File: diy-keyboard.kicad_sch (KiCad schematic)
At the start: 21 parts, among them J1 AVR-ISP-6, SW69 SW_SKQG, U1 PRTR5V0U2X, U2 ATmega32U4-A, Y1 16MHz

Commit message: Re-assign symbol and footprint to match local library
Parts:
- J1: footprint Local_lib_ISP-header:Reset_Pretty-Mask -> Local_Lib:Reset_Pretty-Mask
- USB1: footprint Local_lib_Type-C:HRO-TYPE-C-31-M-12-HandSoldering -> Local_Lib:HRO-TYPE-C-31-M-12-HandSoldering

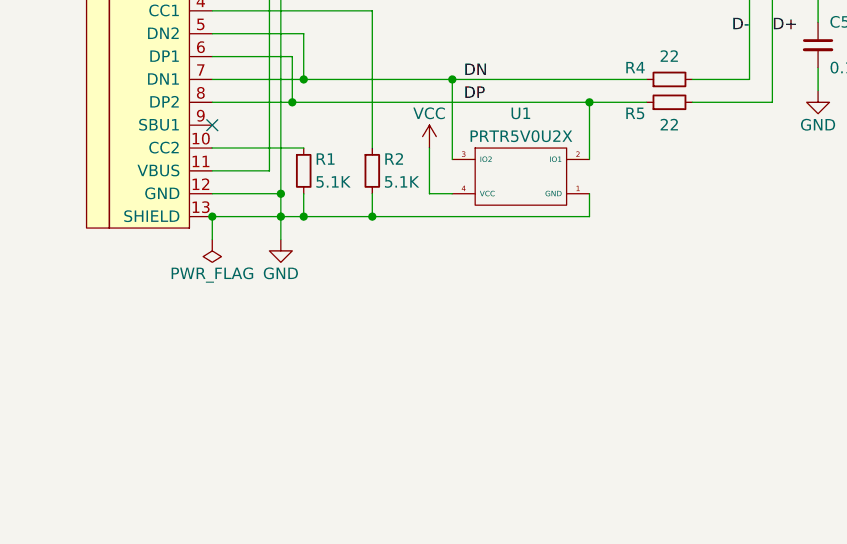
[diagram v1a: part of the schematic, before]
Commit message: Adding ferrite bead to usb sield
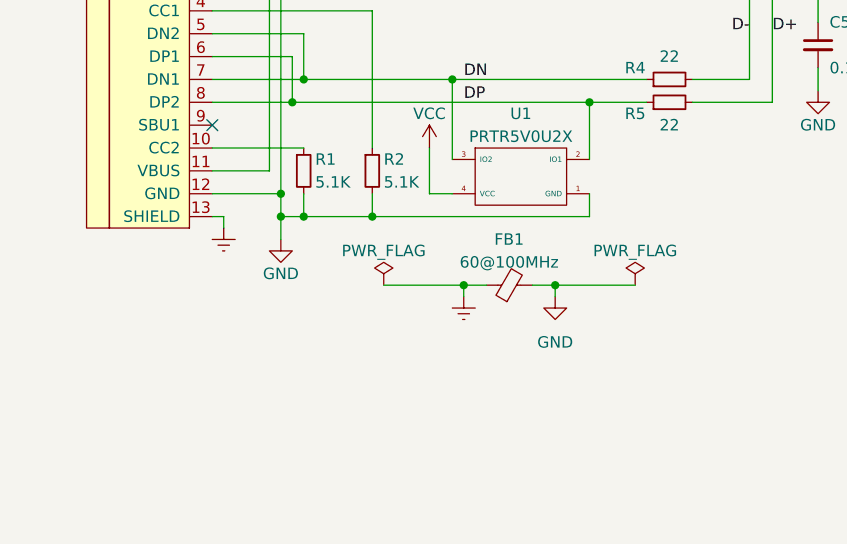
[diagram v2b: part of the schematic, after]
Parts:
- added FB1: 60@100MHz, Inductor_SMD:L_0805_2012Metric_Pad1.15x1.40mm_HandSolder, symbol Device:FerriteBead_Small
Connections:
- net GND: now also FB1.2; no longer USB1.13 (SHIELD)
- new net Earth: FB1.1, USB1.13 (SHIELD)
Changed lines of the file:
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@@
   (junction (at 67.31 120.65) (diameter 0) (color 0 0 0 0)
   )
+  (junction (at 87.63 128.27) (diameter 0) (color 0 0 0 0)
+  )
   (junction (at 104.14 80.01) (diameter 0) (color 0 0 0 0)
   )
@@
   (junction (at 104.14 77.47) (diameter 0) (color 0 0 0 0)
   )
+  (junction (at 97.79 128.27) (diameter 0) (color 0 0 0 0)
+  )
   (junction (at 86.36 92.71) (diameter 0) (color 0 0 0 0)
   )
@@
   )
   (junction (at 67.31 118.11) (diameter 0) (color 0 0 0 0)
-  )
-  (junction (at 59.69 120.65) (diameter 0) (color 0 0 0 0)
   )
   (junction (at 147.32 147.32) (diameter 0) (color 0 0 0 0)
@@
     (stroke (width 0) (type default))
   )
+  (wire (pts (xy 87.63 128.27) (xy 87.63 129.54))
+    (stroke (width 0) (type default))
+  )
   (wire (pts (xy 86.36 90.17) (xy 86.36 92.71))
     (stroke (width 0) (type default))
@@
     (stroke (width 0) (type default))
   )
-  (wire (pts (xy 67.31 120.65) (xy 59.69 120.65))
-    (stroke (width 0) (type default))
-  )
   (wire (pts (xy 163.83 116.84) (xy 173.99 116.84))
     (stroke (width 0) (type default))
@@
     (stroke (width 0) (type default))
   )
+  (wire (pts (xy 60.96 121.92) (xy 60.96 120.65))
+    (stroke (width 0) (type default))
+  )
   (wire (pts (xy 77.47 120.65) (xy 69.85 120.65))
     (stroke (width 0) (type default))
@@
     (stroke (width 0) (type default))
   )
+  (wire (pts (xy 97.79 128.27) (xy 106.68 128.27))
+    (stroke (width 0) (type default))
+  )
   (wire (pts (xy 86.36 105.41) (xy 86.36 114.3))
     (stroke (width 0) (type default))
@@
     (stroke (width 0) (type default))
   )
-  (wire (pts (xy 59.69 120.65) (xy 59.69 123.19))
-    (stroke (width 0) (type default))
-  )
   (wire (pts (xy 87.63 59.69) (xy 87.63 60.96))
     (stroke (width 0) (type default))
@@
     (stroke (width 0) (type default))
   )
+  (wire (pts (xy 78.74 128.27) (xy 87.63 128.27))
+    (stroke (width 0) (type default))
+  )
   (wire (pts (xy 86.36 105.41) (xy 107.95 105.41))
     (stroke (width 0) (type default))
@@
     (stroke (width 0) (type default))
   )
+  (wire (pts (xy 97.79 128.27) (xy 97.79 129.54))
+    (stroke (width 0) (type default))
+  )
   (wire (pts (xy 113.03 68.58) (xy 133.35 68.58))
     (stroke (width 0) (type default))
@@
     (stroke (width 0) (type default))
   )
+  (wire (pts (xy 87.63 128.27) (xy 90.17 128.27))
+    (stroke (width 0) (type default))
+  )
   (wire (pts (xy 214.63 80.01) (xy 218.44 80.01))
     (stroke (width 0) (type default))
@@
     (stroke (width 0) (type default))
   )
+  (wire (pts (xy 60.96 120.65) (xy 59.69 120.65))
+    (stroke (width 0) (type default))
+  )
   (wire (pts (xy 104.14 71.12) (xy 104.14 69.85))
     (stroke (width 0) (type default))
@@
     (stroke (width 0) (type default))
   )
+  (wire (pts (xy 95.25 128.27) (xy 97.79 128.27))
+    (stroke (width 0) (type default))
+  )
   (wire (pts (xy 163.83 104.14) (xy 167.64 104.14))
     (stroke (width 0) (type default))
@@
     )
   )
+  (symbol (lib_id "power:PWR_FLAG") (at 106.68 128.27 0) (unit 1)
+    (in_bom yes) (on_board yes) (dnp no) (fields_autoplaced)
+    (property "Reference" "#FLG04" (at 106.68 126.365 0)
+      (effects (font (size 1.27 1.27)) hide)
+    )
+    (property "Value" "PWR_FLAG" (at 106.68 124.46 0)
+      (effects (font (size 1.27 1.27)))
+    )
+    (property "Footprint" "" (at 106.68 128.27 0)
+      (effects (font (size 1.27 1.27)) hide)
+    )
+    (property "Datasheet" "~" (at 106.68 128.27 0)
+      (effects (font (size 1.27 1.27)) hide)
+    )
+    (pin "1")
+    (instances
+      (project "diy-keyboard"
+        (path "/61c1c9ec-fe7c-471e-87ac-8564e079edaa"
+          (reference "#FLG04") (unit 1)
+        )
+      )
+    )
+  )
   (symbol (lib_id "Device:R_Small") (at 176.53 116.84 90) (unit 1)
     (in_bom yes) (on_board yes) (dnp no)
@@
     )
   )
-  (symbol (lib_id "power:PWR_FLAG") (at 59.69 123.19 180) (unit 1)
-    (in_bom yes) (on_board yes) (dnp no)
-    (property "Reference" "#FLG01" (at 59.69 125.095 0)
-      (effects (font (size 1.27 1.27)) hide)
-    )
-    (property "Value" "PWR_FLAG" (at 59.69 127 0)
-      (effects (font (size 1.27 1.27)))
-    )
-    (property "Footprint" "" (at 59.69 123.19 0)
-      (effects (font (size 1.27 1.27)) hide)
-    )
-    (property "Datasheet" "~" (at 59.69 123.19 0)
+  (symbol (lib_id "power:PWR_FLAG") (at 78.74 128.27 0) (unit 1)
+    (in_bom yes) (on_board yes) (dnp no)
+    (property "Reference" "#FLG01" (at 78.74 126.365 0)
+      (effects (font (size 1.27 1.27)) hide)
+    )
+    (property "Value" "PWR_FLAG" (at 78.74 124.46 0)
+      (effects (font (size 1.27 1.27)))
+    )
+    (property "Footprint" "" (at 78.74 128.27 0)
+      (effects (font (size 1.27 1.27)) hide)
+    )
+    (property "Datasheet" "~" (at 78.74 128.27 0)
       (effects (font (size 1.27 1.27)) hide)
     )
@@
     )
   )
+  (symbol (lib_id "power:GND") (at 97.79 129.54 0) (unit 1)
+    (in_bom yes) (on_board yes) (dnp no) (fields_autoplaced)
+    (property "Reference" "#PWR018" (at 97.79 135.89 0)
+      (effects (font (size 1.27 1.27)) hide)
+    )
+    (property "Value" "GND" (at 97.79 134.62 0)
+      (effects (font (size 1.27 1.27)))
+    )
+    (property "Footprint" "" (at 97.79 129.54 0)
+      (effects (font (size 1.27 1.27)) hide)
+    )
+    (property "Datasheet" "" (at 97.79 129.54 0)
+      (effects (font (size 1.27 1.27)) hide)
+    )
+    (pin "1")
+    (instances
+      (project "diy-keyboard"
+        (path "/61c1c9ec-fe7c-471e-87ac-8564e079edaa"
+          (reference "#PWR018") (unit 1)
+        )
+      )
+    )
+  )
   (symbol (lib_id "Device:C_Small") (at 137.16 41.91 0) (unit 1)
     (in_bom yes) (on_board yes) (dnp no)
@@
         (path "/61c1c9ec-fe7c-471e-87ac-8564e079edaa"
           (reference "#PWR013") (unit 1)
+        )
+      )
+    )
+  )
+  (symbol (lib_id "Device:FerriteBead_Small") (at 92.71 128.27 90) (unit 1)
+    (in_bom yes) (on_board yes) (dnp no) (fields_autoplaced)
+    (property "Reference" "FB1" (at 92.6719 123.19 90)
+      (effects (font (size 1.27 1.27)))
+    )
+    (property "Value" "60@100MHz" (at 92.6719 125.73 90)
+      (effects (font (size 1.27 1.27)))
+    )
+    (property "Footprint" "Inductor_SMD:L_0805_2012Metric_Pad1.15x1.40mm_HandSolder" (at 92.71 130.048 90)
+      (effects (font (size 1.27 1.27)) hide)
+    )
+    (property "Datasheet" "~" (at 92.71 128.27 0)
+      (effects (font (size 1.27 1.27)) hide)
+    )
+    (pin "1")
+    (pin "2")
+    (instances
+      (project "diy-keyboard"
+        (path "/61c1c9ec-fe7c-471e-87ac-8564e079edaa"
+          (reference "FB1") (unit 1)
         )
       )
@@
         (path "/61c1c9ec-fe7c-471e-87ac-8564e079edaa"
           (reference "#FLG03") (unit 1)
+        )
+      )
+    )
+  )
+  (symbol (lib_id "power:Earth") (at 87.63 129.54 0) (mirror y) (unit 1)
+    (in_bom yes) (on_board yes) (dnp no)
+    (property "Reference" "#PWR017" (at 87.63 135.89 0)
+      (effects (font (size 1.27 1.27)) hide)
+    )
+    (property "Value" "Earth" (at 87.63 133.35 0)
+      (effects (font (size 1.27 1.27)) hide)
+    )
+    (property "Footprint" "" (at 87.63 129.54 0)
+      (effects (font (size 1.27 1.27)) hide)
+    )
+    (property "Datasheet" "~" (at 87.63 129.54 0)
+      (effects (font (size 1.27 1.27)) hide)
+    )
+    (pin "1")
+    (instances
+      (project "diy-keyboard"
+        (path "/61c1c9ec-fe7c-471e-87ac-8564e079edaa"
+          (reference "#PWR017") (unit 1)
         )
       )
@@
         )
       )
+    )
+  )
+  (symbol (lib_id "power:Earth") (at 60.96 121.92 0) (unit 1)
+    (in_bom yes) (on_board yes) (dnp no) (fields_autoplaced)
+    (property "Reference" "#PWR019" (at 60.96 128.27 0)
+      (effects (font (size 1.27 1.27)) hide)
+    )
+    (property "Value" "Earth" (at 60.96 125.73 0)
+      (effects (font (size 1.27 1.27)) hide)
+    )
+    (property "Footprint" "" (at 60.96 121.92 0)
+      (effects (font (size 1.27 1.27)) hide)
+    )
+    (property "Datasheet" "~" (at 60.96 121.92 0)
+      (effects (font (size 1.27 1.27)) hide)
+    )
+    (pin "1")
+    (instances
+      (project "diy-keyboard"
+        (path "/61c1c9ec-fe7c-471e-87ac-8564e079edaa"
+          (reference "#PWR019") (unit 1)
+        )
+      )
